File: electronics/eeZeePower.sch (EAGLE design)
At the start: 11 parts

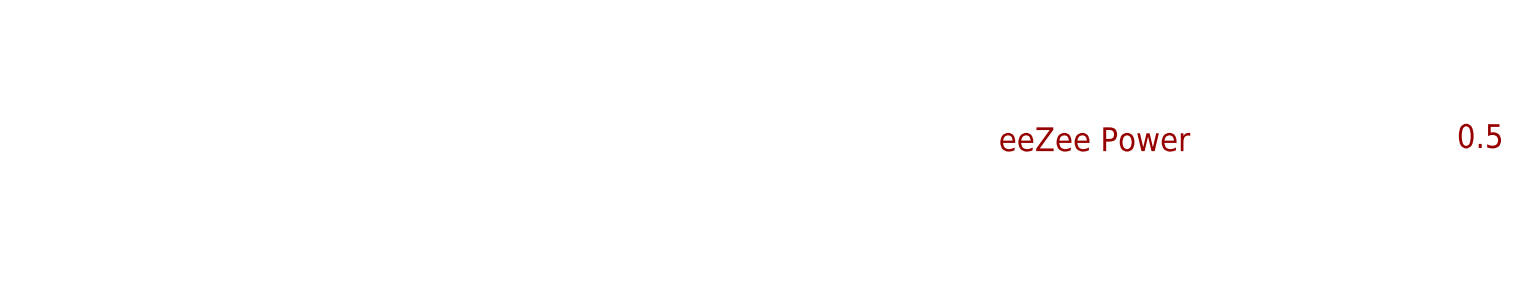
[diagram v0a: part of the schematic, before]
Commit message: minib: replaced logo; moved power select headers, passives; added help url; updated gerbers, zip
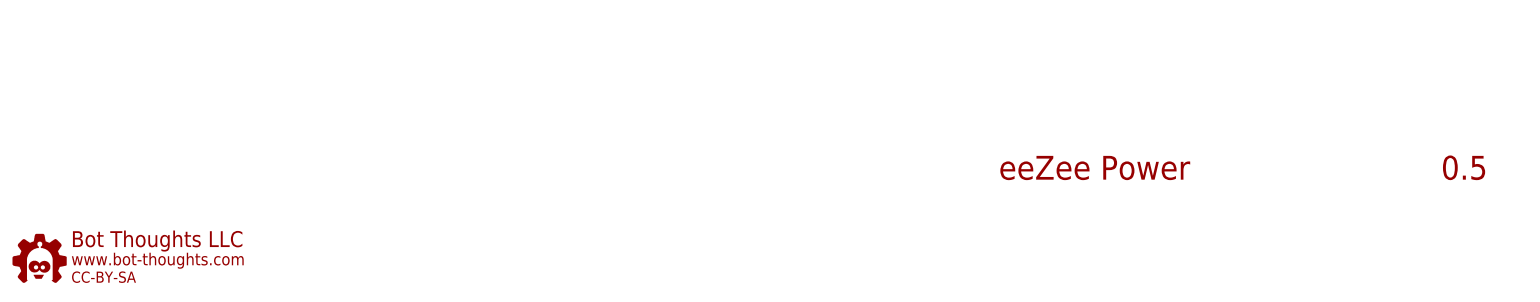
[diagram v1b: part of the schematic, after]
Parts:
- added U$2: BTLOGO-LOGO-MD, bt:BTLOGO-LOGO-MD
